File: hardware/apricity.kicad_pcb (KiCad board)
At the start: 2 copper layers, 71.2 x 71.2 mm, 37 parts, among them J1 Conn_01x03_Male, J2 USB_C_Receptacle_USB2.0, SW1 Reset, SW2 Prog, U1 ESP-WROOM-02D, U2 AP2210N-3.3TRG1

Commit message: capitalize button labels
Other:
- board text added: "PROG"
- board text added: "RESET"
- board text removed: "Prog"
- board text removed: "Reset"
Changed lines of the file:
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@@
     (effects (font (size 1 1) (thickness 0.15)))
   )
-  (gr_text "Reset\n" (at 147.975 115.5) (layer "F.SilkS")
+  (gr_text "RESET\n" (at 147.975 115.5) (layer "F.SilkS")
     (effects (font (size 1 1) (thickness 0.15)))
   )
-  (gr_text "Prog\n\n\n" (at 158.225 113.125) (layer "F.SilkS")
+  (gr_text "PROG" (at 158.1 111.5) (layer "F.SilkS")
     (effects (font (size 1 1) (thickness 0.15)))
   )

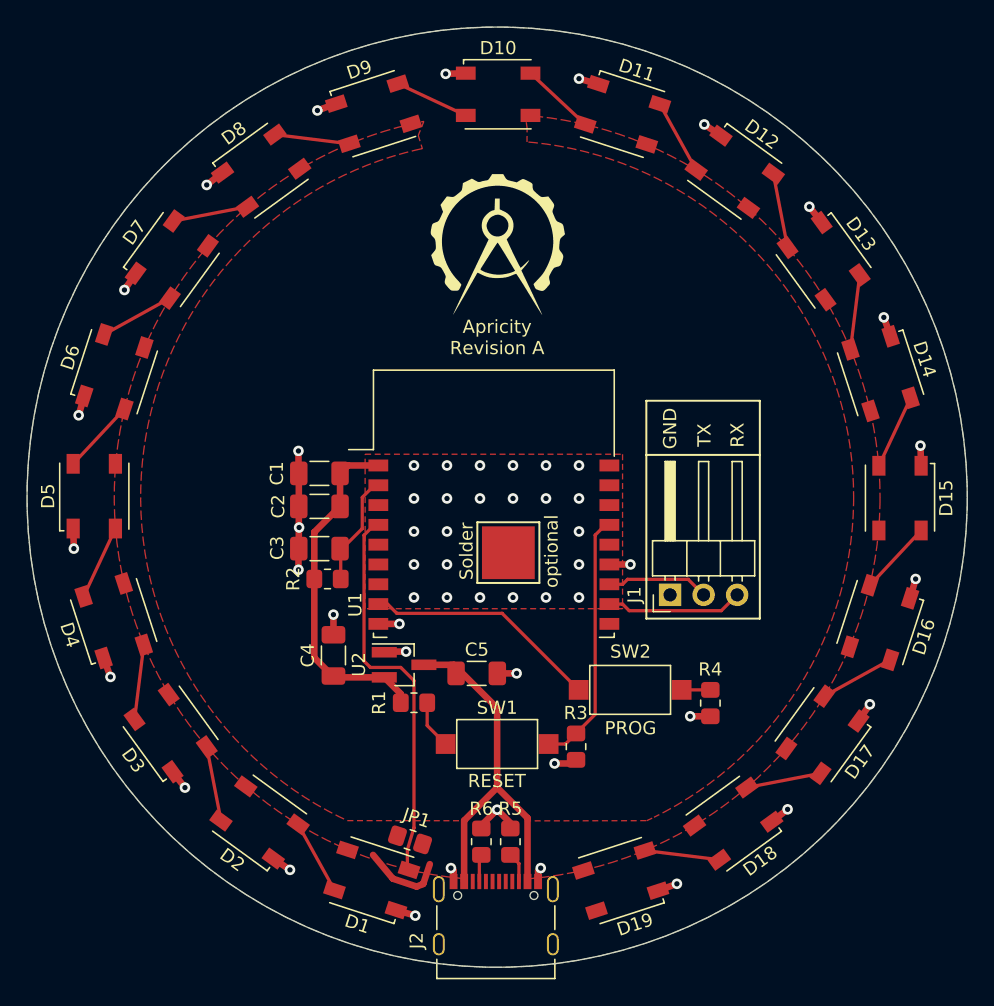
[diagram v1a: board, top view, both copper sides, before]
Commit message: replace zones with traces
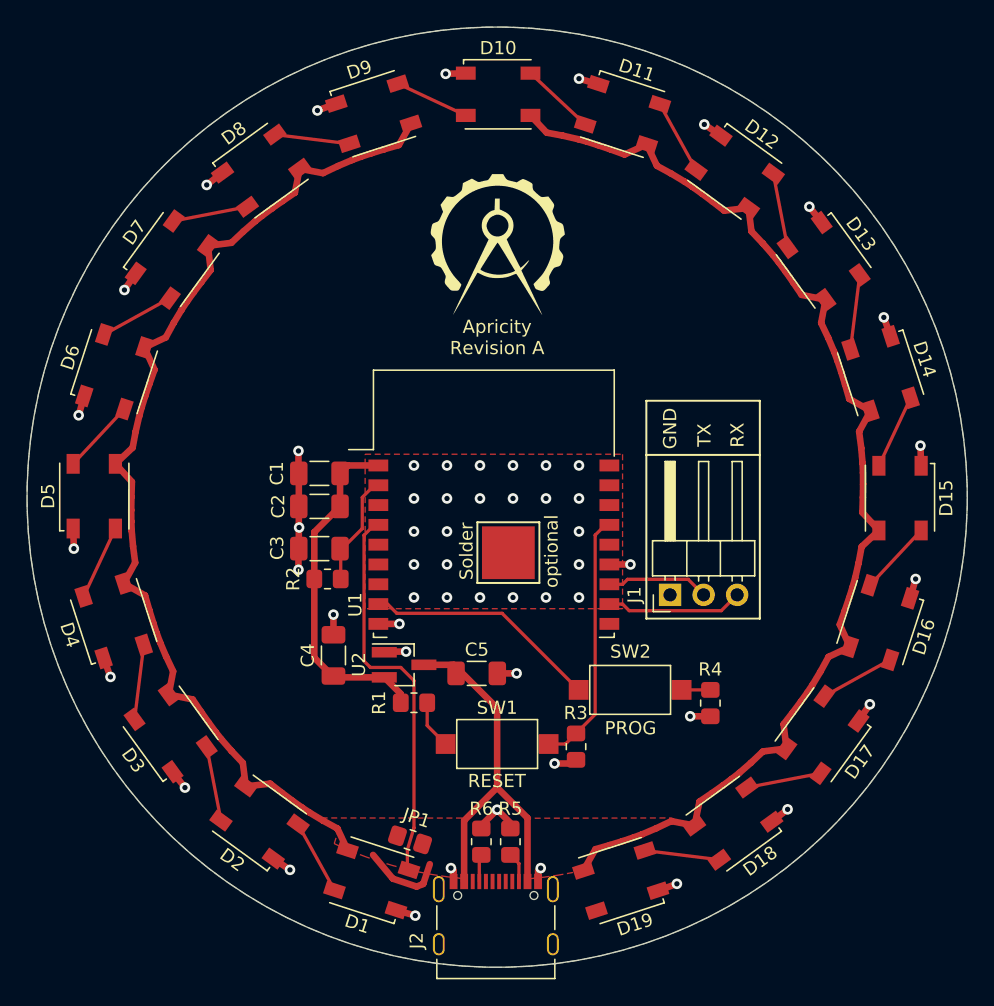
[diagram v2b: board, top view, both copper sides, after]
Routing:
- net +5V: track 35.5 -> 201.8 mm

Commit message: add capacitors for LEDs
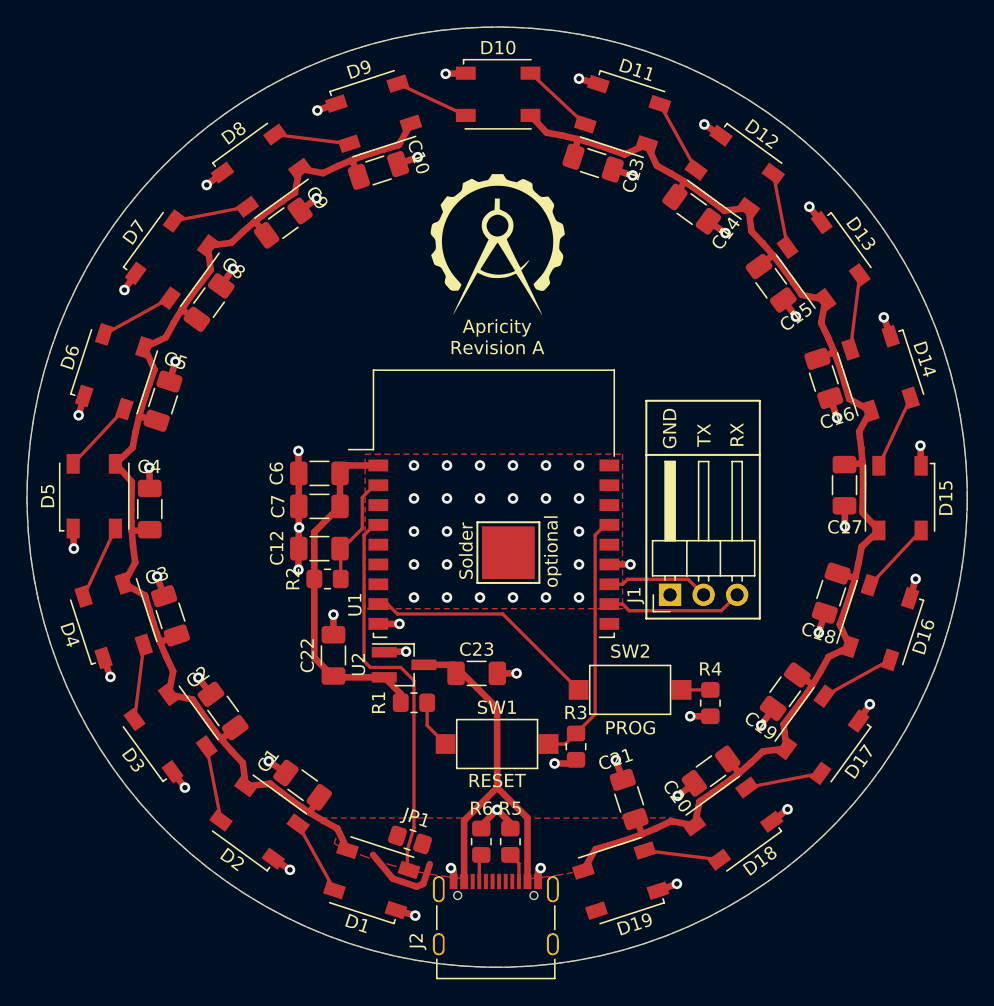
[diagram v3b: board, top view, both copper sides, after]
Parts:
- added C1: 0.1u, Capacitor_SMD:C_1206_3216Metric_Pad1.33x1.80mm_HandSolder, F.Cu at (133.3, 115.8)
- added C10: 0.1u, Capacitor_SMD:C_1206_3216Metric_Pad1.33x1.80mm_HandSolder, F.Cu at (139.0, 69.3)
- added C13: 0.1u, Capacitor_SMD:C_1206_3216Metric_Pad1.33x1.80mm_HandSolder, F.Cu at (155.3, 68.7)
- added C14: 0.1u, Capacitor_SMD:C_1206_3216Metric_Pad1.33x1.80mm_HandSolder, F.Cu at (162.7, 72.2)
- added C15: 0.1u, Capacitor_SMD:C_1206_3216Metric_Pad1.33x1.80mm_HandSolder, F.Cu at (168.8, 77.8)
- added C16: 0.1u, Capacitor_SMD:C_1206_3216Metric_Pad1.33x1.80mm_HandSolder, F.Cu at (172.7, 85.0)
- added C17: 0.1u, Capacitor_SMD:C_1206_3216Metric_Pad1.33x1.80mm_HandSolder, F.Cu at (174.3, 93.1)
- added C18: 0.1u, Capacitor_SMD:C_1206_3216Metric_Pad1.33x1.80mm_HandSolder, F.Cu at (173.3, 101.3)
- added C19: 0.1u, Capacitor_SMD:C_1206_3216Metric_Pad1.33x1.80mm_HandSolder, F.Cu at (169.8, 108.7)
- added C2: 0.1u, Capacitor_SMD:C_1206_3216Metric_Pad1.33x1.80mm_HandSolder, F.Cu at (127.2, 110.2)
- added C20: 0.1u, Capacitor_SMD:C_1206_3216Metric_Pad1.33x1.80mm_HandSolder, F.Cu at (164.2, 114.8)
- added C21: 0.1u, Capacitor_SMD:C_1206_3216Metric_Pad1.33x1.80mm_HandSolder, F.Cu at (158.0, 116.9)
- added C3: 0.1u, Capacitor_SMD:C_1206_3216Metric_Pad1.33x1.80mm_HandSolder, F.Cu at (123.3, 103.0)
- added C4: 0.1u, Capacitor_SMD:C_1206_3216Metric_Pad1.33x1.80mm_HandSolder, F.Cu at (121.7, 94.9)
- added C5: 0.1u, Capacitor_SMD:C_1206_3216Metric_Pad1.33x1.80mm_HandSolder, F.Cu at (122.7, 86.7)
- added C8: 0.1u, Capacitor_SMD:C_1206_3216Metric_Pad1.33x1.80mm_HandSolder, F.Cu at (126.2, 79.3)
- added C9: 0.1u, Capacitor_SMD:C_1206_3216Metric_Pad1.33x1.80mm_HandSolder, F.Cu at (131.8, 73.2)
- renumbered C3 to C12, C4 to C22, C5 to C23, C1 to C6, C2 to C7
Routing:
- net GND: track 55.2 -> 82.1 mm, vias 56 -> 73
- net +5V: track 201.8 -> 225.2 mm

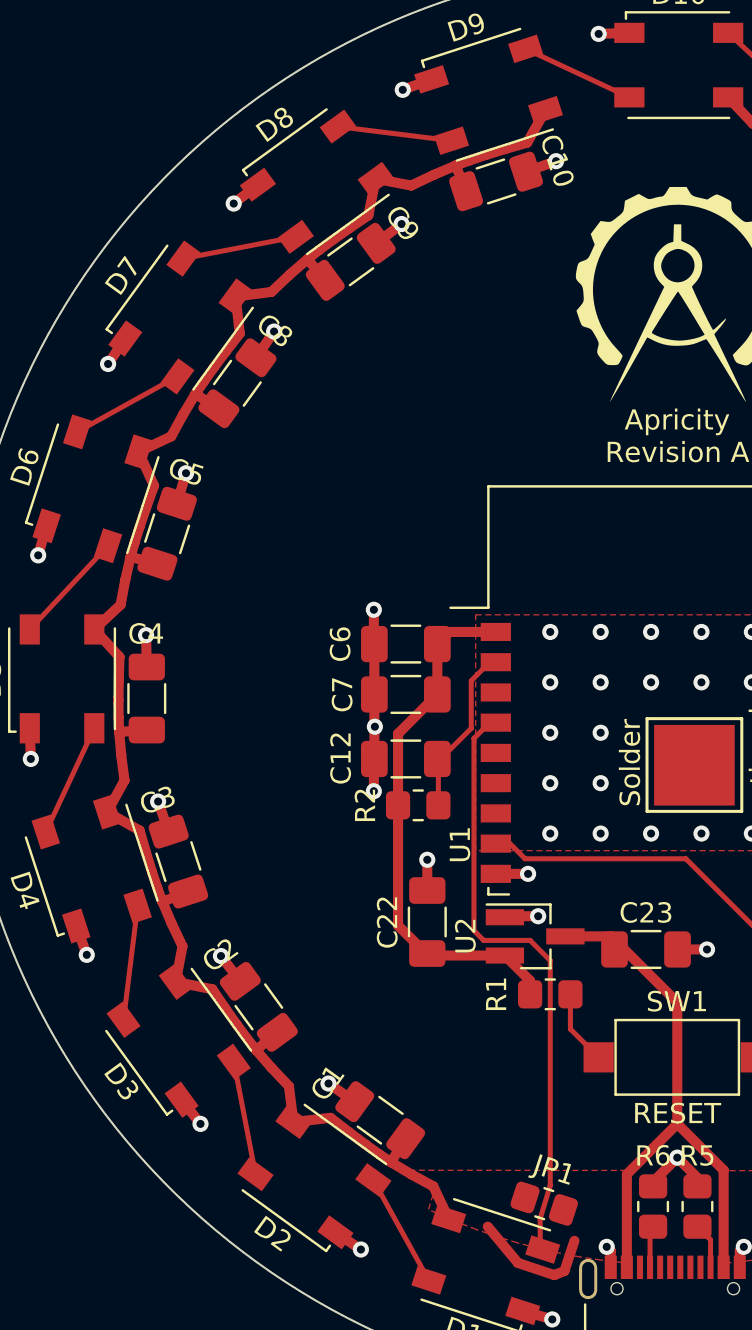
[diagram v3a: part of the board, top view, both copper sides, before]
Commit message: add back in capacitor for D1
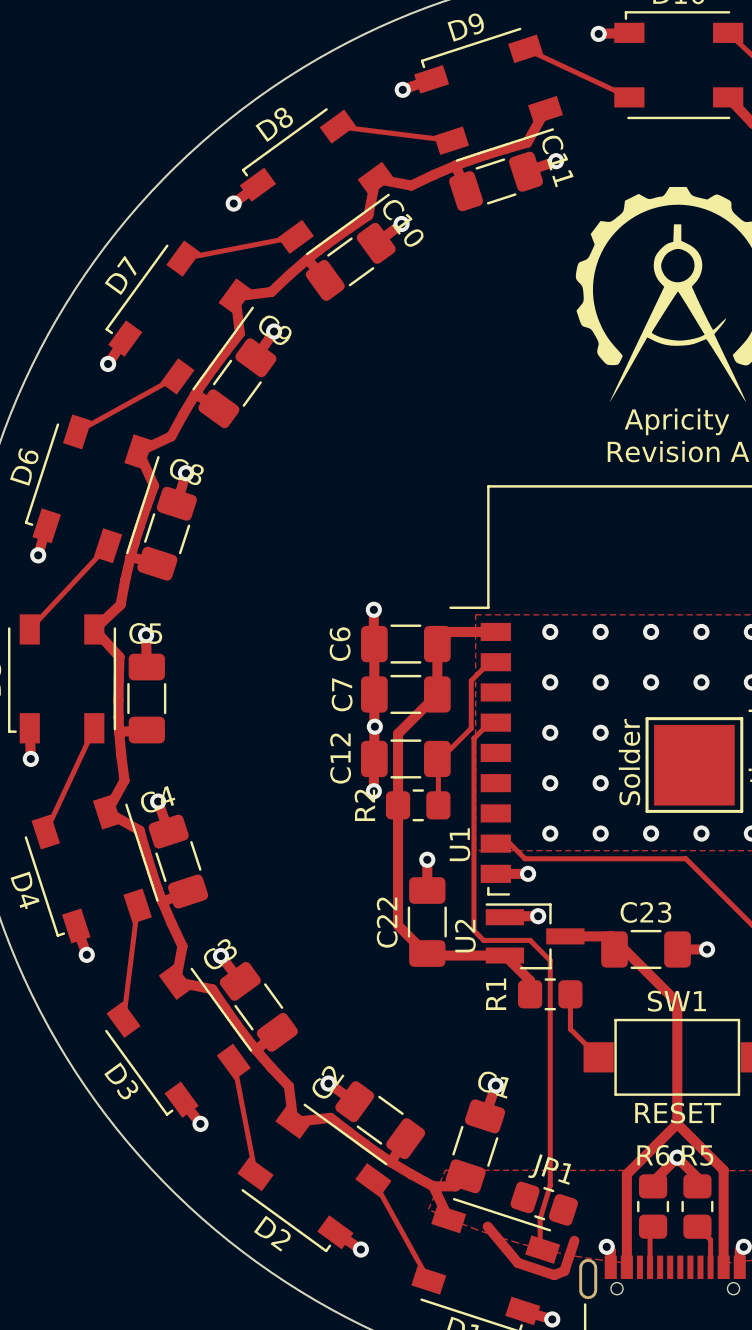
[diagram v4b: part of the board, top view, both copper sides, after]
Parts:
- added C1: 0.1u, Capacitor_SMD:C_1206_3216Metric_Pad1.33x1.80mm_HandSolder, F.Cu at (138.0, 117.1)
- renumbered C9 to C10, C10 to C11, C1 to C2, C2 to C3, C3 to C4, C4 to C5, C5 to C8, C8 to C9
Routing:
- net +5V: track 225.2 -> 227.0 mm
- net GND: track 82.1 -> 83.7 mm, vias 73 -> 74
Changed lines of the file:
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@@
     (property "Sheetname" "")
     (attr smd)
-    (fp_text reference "C4" (at 3.190847 -0.03156) (layer "F.SilkS")
+    (fp_text reference "C5" (at 3.190847 -0.03156) (layer "F.SilkS")
       (effects (font (size 1 1) (thickness 0.15)))
     )
@@
     (property "Sheetname" "")
     (attr smd)
-    (fp_text reference "C3" (at 3.190847 -0.03156 18) (layer "F.SilkS")
+    (fp_text reference "C4" (at 3.190847 -0.03156 18) (layer "F.SilkS")
       (effects (font (size 1 1) (thickness 0.15)))
     )
@@
     (property "Sheetname" "")
     (attr smd)
-    (fp_text reference "C8" (at 3.190847 -0.03156 144) (layer "F.SilkS")
+    (fp_text reference "C9" (at 3.190847 -0.03156 144) (layer "F.SilkS")
       (effects (font (size 1 1) (thickness 0.15)))
     )
@@
     (property "Sheetname" "")
     (attr smd)
-    (fp_text reference "C5" (at 3.190847 -0.03156 162) (layer "F.SilkS")
+    (fp_text reference "C8" (at 3.190847 -0.031559 162) (layer "F.SilkS")
       (effects (font (size 1 1) (thickness 0.15)))
     )
@@
     (property "Sheetname" "")
     (attr smd)
-    (fp_text reference "C9" (at 3.190847 -0.03156 126) (layer "F.SilkS")
+    (fp_text reference "C10" (at 3.190847 -0.03156 126) (layer "F.SilkS")
       (effects (font (size 1 1) (thickness 0.15)))
     )
@@
     )
   )
+  (footprint "Capacitor_SMD:C_1206_3216Metric_Pad1.33x1.80mm_HandSolder" (layer "F.Cu")
+    (at 137.982839 117.113974 72)
+    (descr "Capacitor SMD 1206 (3216 Metric), square (rectangular) end terminal, IPC_7351 nominal with elongated pad for handsoldering. (Body size source: IPC-SM-782 page 76, https://www.pcb-3d.com/wordpress/wp-content/uploads/ipc-sm-782a_amendment_1_and_2.pdf), generated with kicad-footprint-generator")
+    (tags "capacitor handsolder")
+    (property "Sheetfile" "apricity.kicad_sch")
+    (property "Sheetname" "")
+    (attr smd)
+    (fp_text reference "C1" (at 3.190847 -0.031559 162) (layer "F.SilkS")
+      (effects (font (size 1 1) (thickness 0.15)))
+    )
+    (fp_text value "0.1u" (at 0 1.85 72) (layer "F.Fab")
+      (effects (font (size 1 1) (thickness 0.15)))
+    )
+    (fp_text user "${REFERENCE}" (at 0 0 72) (layer "F.Fab")
+      (effects (font (size 0.8 0.8) (thickness 0.12)))
+    )
+    (fp_line (start -0.711252 0.91) (end 0.711252 0.91) (layer "F.SilkS") (width 0.12))
+    (fp_line (start -0.711252 -0.91) (end 0.711252 -0.91) (layer "F.SilkS") (width 0.12))
+    (fp_line (start 2.48 -1.15) (end 2.48 1.15) (layer "F.CrtYd") (width 0.05))
+    (fp_line (start -2.48 -1.15) (end 2.48 -1.15) (layer "F.CrtYd") (width 0.05))
+    (fp_line (start -2.48 1.15) (end -2.48 -1.15) (layer "F.CrtYd") (width 0.05))
+    (fp_line (start 2.48 1.15) (end -2.48 1.15) (layer "F.CrtYd") (width 0.05))
+    (fp_line (start 1.6 0.8) (end -1.6 0.8) (layer "F.Fab") (width 0.1))
+    (fp_line (start -1.6 -0.8) (end 1.6 -0.8) (layer "F.Fab") (width 0.1))
+    (fp_line (start -1.6 0.8) (end -1.6 -0.8) (layer "F.Fab") (width 0.1))
+    (fp_line (start 1.6 -0.8) (end 1.6 0.8) (layer "F.Fab") (width 0.1))
+    (pad "1" smd roundrect (at -1.5625 0 72) (size 1.325 1.8) (layers "F.Cu" "F.Paste" "F.Mask") (roundrect_rratio 0.188679)
+      (net 2 "+5V") (pintype "passive"))
+    (pad "2" smd roundrect (at 1.5625 0 72) (size 1.325 1.8) (layers "F.Cu" "F.Paste" "F.Mask") (roundrect_rratio 0.188679)
+      (net 1 "GND") (pintype "passive"))
+    (model "${KICAD6_3DMODEL_DIR}/Capacitor_SMD.3dshapes/C_1206_3216Metric.wrl"
+      (offset (xyz 0 0 0))
+      (scale (xyz 1 1 1))
+      (rotate (xyz 0 0 0))
+    )
+  )
   (footprint "Resistor_SMD:R_0805_2012Metric_Pad1.20x1.40mm_HandSolder" (layer "F.Cu")
     (at 146.8 120.1 90)
@@
     (property "Sheetname" "")
     (attr smd)
-    (fp_text reference "C2" (at 3.190847 -0.03156 36) (layer "F.SilkS")
+    (fp_text reference "C3" (at 3.190847 -0.03156 36) (layer "F.SilkS")
       (effects (font (size 1 1) (thickness 0.15)))
     )
@@
     (property "Sheetname" "")
     (attr smd)
-    (fp_text reference "C1" (at 3.190847 -0.03156 54) (layer "F.SilkS")
+    (fp_text reference "C2" (at 3.190847 -0.03156 54) (layer "F.SilkS")
       (effects (font (size 1 1) (thickness 0.15)))
     )
@@
     (property "Sheetname" "")
     (attr smd)
-    (fp_text reference "C10" (at 3.190847 -0.03156 108) (layer "F.SilkS")
+    (fp_text reference "C11" (at 3.190847 -0.03156 108) (layer "F.SilkS")
       (effects (font (size 1 1) (thickness 0.15)))
     )
@@
   (segment (start 149.1 119.1) (end 149.1 118.775) (width 0.5) (layer "F.Cu") (net 1))
   (segment (start 146.9 118.775) (end 148 117.675) (width 0.5) (layer "F.Cu") (net 1))
+  (segment (start 139 114.1) (end 138.465678 115.627948) (width 0.5) (layer "F.Cu") (net 1))
   (segment (start 149.1 118.775) (end 148 117.675) (width 0.5) (layer "F.Cu") (net 1))
   (segment (start 161.616887 123.290107) (end 160.184627 123.810052) (width 0.5) (layer "F.Cu") (net 1))
@@
   (via (at 170.00157 117.648698) (size 0.8) (drill 0.4) (layers "F.Cu" "B.Cu") (free) (net 1))
   (via (at 156.994445 113.921738) (size 0.8) (drill 0.4) (layers "F.Cu" "B.Cu") (free) (net 1))
+  (via (at 139 114.1) (size 0.8) (drill 0.4) (layers "F.Cu" "B.Cu") (free) (net 1))
   (via (at 141.1 105.7) (size 0.8) (drill 0.4) (layers "F.Cu" "B.Cu") (free) (net 1))
   (via (at 163.692389 65.767414) (size 0.8) (drill 0.4) (layers "F.Cu" "B.Cu") (free) (net 1))
@@
   (segment (start 158.475942 118.263305) (end 158.988956 119.536109) (width 0.5) (layer "F.Cu") (net 2))
   (segment (start 122.9 81.9) (end 123.5 80.8) (width 0.5) (layer "F.Cu") (net 2))
+  (segment (start 137 119.1) (end 135.9 119.1) (width 0.5) (layer "F.Cu") (net 2))
   (segment (start 124.1 79.8) (end 124.5 79.2) (width 0.5) (layer "F.Cu") (net 2))
   (segment (start 148 109.975) (end 148 116) (width 0.5) (layer "F.Cu") (net 2))
@@
   (segment (start 174.670032 86.554238) (end 176.280854 87.464405) (width 0.5) (layer "F.Cu") (net 2))
   (segment (start 165.2 72.300001) (end 167.038165 72.089524) (width 0.5) (layer "F.Cu") (net 2))
+  (segment (start 137.5 118.6) (end 137 119.1) (width 0.5) (layer "F.Cu") (net 2))
   (segment (start 167.83853 76.539014) (end 168.890508 75.657791) (width 0.5) (layer "F.Cu") (net 2))
   (segment (start 141.2 122.110885) (end 141.324516 122.235401) (width 0.25) (layer "F.Cu") (net 3))
@@
         (xy 136.064045 120.435209)
         (xy 135.660479 120.244013)
-        (xy 136 119.15)
-        (xy 134.703669 118.30112)
+        (xy 136.5 118.3)
       )
     )
